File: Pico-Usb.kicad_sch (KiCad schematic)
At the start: 40 parts, among them J1 USB_A, J3 MEM2067-02-180-00-A_REVB, J4 10133475-10001LF, SW1 SW_Push, SW2 SW_Push, SW3 SW_Push, SW4 A6H-4101, U1 RP2040, U2 W25Q128JVS, U3 MAX40200AUK, U4 MAX40200AUK, U5 AP2112K-3.3, U6 TS3USB221ARSER, Y2 ABM3B-12.000MHZ-10-1-U-T

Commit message: Elimine todas las pistas y acomode los componetes
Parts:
- renumbered SW2 to BOOTSEL, SW3 to MODE, SW1 to RST
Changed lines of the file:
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@@
 		(dnp no)
 		(fields_autoplaced yes)
-		(property "Reference" "SW2"
+		(property "Reference" "BOOTSEL"
 			(at 182.88 69.85 0)
 			(show_name no)
@@
 			(project "Pico-Usb"
 				(path "/e96aad04-5f72-44f4-a95f-714a14090504"
-					(reference "SW2")
+					(reference "BOOTSEL")
 					(unit 1)
 				)
@@
 		(dnp no)
 		(fields_autoplaced yes)
-		(property "Reference" "SW1"
+		(property "Reference" "RST"
 			(at 39.37 132.08 0)
 			(show_name no)
@@
 			(project "Pico-Usb"
 				(path "/e96aad04-5f72-44f4-a95f-714a14090504"
-					(reference "SW1")
+					(reference "RST")
 					(unit 1)
 				)
@@
 		(dnp no)
 		(fields_autoplaced yes)
-		(property "Reference" "SW3"
-			(at 113.0299 123.19 90)
+		(property "Reference" "MODE"
+			(at 114.3 119.38 0)
 			(show_name no)
 			(do_not_autoplace no)
@@
 					(size 1.27 1.27)
 				)
-				(justify right)
 			)
 		)
 		(property "Value" "SW_Push"
-			(at 115.5699 123.19 90)
+			(at 114.3 121.92 0)
 			(show_name no)
 			(do_not_autoplace no)
@@
 					(size 1.27 1.27)
 				)
-				(justify right)
 			)
 		)
@@
 			(project "Pico-Usb"
 				(path "/e96aad04-5f72-44f4-a95f-714a14090504"
-					(reference "SW3")
+					(reference "MODE")
 					(unit 1)
 				)

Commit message: Termine el ruteo
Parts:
- renumbered SW4 to CFG
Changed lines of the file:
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@@
 		(dnp no)
 		(fields_autoplaced yes)
-		(property "Reference" "SW4"
+		(property "Reference" "CFG"
 			(at 205.7304 229.87 0)
 			(show_name no)
@@
 			(project "Pico-Usb"
 				(path "/e96aad04-5f72-44f4-a95f-714a14090504"
-					(reference "SW4")
+					(reference "CFG")
 					(unit 1)
 				)

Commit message: Corregi valores
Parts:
- C10, C11, C13: value 10μF -> 10uF
- C5, C7: value 1μF -> 1uF
- R2, R3: value 28 -> 28R
- R7, R8: value 5.1k -> 5k1
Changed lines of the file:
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@@
 			)
 		)
-		(property "Value" "28"
+		(property "Value" "28R"
 			(at 48.26 151.892 90)
 			(show_name no)
@@
 			)
 		)
-		(property "Value" "28"
+		(property "Value" "28R"
 			(at 48.26 145.288 90)
 			(show_name no)
@@
 			)
 		)
-		(property "Value" "5.1k"
+		(property "Value" "5k1"
 			(at 323.596 92.964 0)
 			(show_name no)
@@
 			)
 		)
-		(property "Value" "1μF"
+		(property "Value" "1uF"
 			(at 94.742 102.87 90)
 			(show_name no)
@@
 			)
 		)
-		(property "Value" "10μF"
+		(property "Value" "10uF"
 			(at 369.316 142.24 0)
 			(show_name no)
@@
 			)
 		)
-		(property "Value" "1μF"
+		(property "Value" "1uF"
 			(at 85.344 99.822 90)
 			(show_name no)
@@
 			)
 		)
-		(property "Value" "10μF"
+		(property "Value" "10uF"
 			(at 338.836 143.256 0)
 			(show_name no)
@@
 			)
 		)
-		(property "Value" "10μF"
+		(property "Value" "10uF"
 			(at 199.136 175.26 0)
 			(show_name no)
@@
 			)
 		)
-		(property "Value" "5.1k"
+		(property "Value" "5k1"
 			(at 377.444 108.966 0)
 			(show_name no)

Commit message: Corregi valores y pistas ground faltantes
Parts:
- renumbered BOOTSEL to BOOTSEL1, C6 to C1, C2 to C10, C12 to C11, C13 to C12, C1 to C13, C9 to C2, C8 to C3, C7 to C6, C3 to C7, C11 to C8, C10 to C9, CFG to CFG1, J4 to J2, MODE to MODE1, R6 to R1, R13 to R10, R1 to R11, R9 to R12, R10 to R13, R5 to R2, R7 to R3, R8 to R4, R4 to R5, R3 to R6, R2 to R7, R11 to R8, R12 to R9, RST to RST1, U3 to U1, U4 to U2, U2 to U3, U5 to U4, U1 to U5, Y2 to Y1

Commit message: Cambie el usb A
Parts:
- removed J1: USB_A, Connector_USB:USB_A_CNCTech_1001-011-01101_Horizontal, symbol Connector:USB_A
- added USB1: USB_AM_180-WT, Custom_Connectors:USB-AM-180-WT, symbol USB_AM_180-WT:USB_AM_180-WT
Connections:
- net GND: now also USB1.4 (GND), USB1.5 (SHELL), USB1.6 (SHELL)
- net USB_A_D+: now also USB1.3 (D+)
- net USB_A_D-: now also USB1.2 (D-)
- net at U1.1 (VDD), U1.3 (EN): now also USB1.1 (VBUS)
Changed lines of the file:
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@@
 	)
 	(junction
+		(at 316.23 34.29)
+		(diameter 0)
+		(color 0 0 0 0)
+	)
+	(junction
 		(at 367.03 39.37)
 		(diameter 0)
@@
 	)
 	(junction
+		(at 316.23 26.67)
+		(diameter 0)
+		(color 0 0 0 0)
+	)
+	(junction
 		(at 198.12 240.03)
 		(diameter 0)
@@
 	)
 	(junction
-		(at 331.47 39.37)
-		(diameter 0)
-		(color 0 0 0 0)
-	)
-	(junction
 		(at 25.4 170.18)
 		(diameter 0)
@@
 	(wire
 		(pts
-			(xy 339.09 24.13) (xy 364.49 24.13)
+			(xy 48.26 128.27) (xy 48.26 130.81)
 		)
 		(stroke
@@
 	(wire
 		(pts
-			(xy 48.26 128.27) (xy 48.26 130.81)
+			(xy 340.36 16.51) (xy 316.23 16.51)
 		)
 		(stroke
@@
 	(wire
 		(pts
+			(xy 339.09 34.29) (xy 364.49 34.29)
+		)
+		(stroke
+			(width 0)
+			(type default)
+		)
+	)
+	(wire
+		(pts
 			(xy 224.79 163.83) (xy 224.79 168.91)
 		)
@@
 	(wire
 		(pts
+			(xy 339.09 26.67) (xy 340.36 26.67)
+		)
+		(stroke
+			(width 0)
+			(type default)
+		)
+	)
+	(wire
+		(pts
 			(xy 364.49 24.13) (xy 370.84 24.13)
 		)
@@
 	(wire
 		(pts
+			(xy 364.49 34.29) (xy 364.49 24.13)
+		)
+		(stroke
+			(width 0)
+			(type default)
+		)
+	)
+	(wire
+		(pts
 			(xy 43.18 187.96) (xy 43.18 193.04)
 		)
@@
 	(wire
 		(pts
+			(xy 340.36 26.67) (xy 340.36 16.51)
+		)
+		(stroke
+			(width 0)
+			(type default)
+		)
+	)
+	(wire
+		(pts
 			(xy 336.55 149.86) (xy 344.17 149.86)
 		)
@@
 	(wire
 		(pts
+			(xy 316.23 34.29) (xy 316.23 39.37)
+		)
+		(stroke
+			(width 0)
+			(type default)
+		)
+	)
+	(wire
+		(pts
 			(xy 78.74 111.76) (xy 78.74 106.68)
 		)
@@
 	(wire
 		(pts
-			(xy 331.47 39.37) (xy 367.03 39.37)
-		)
-		(stroke
-			(width 0)
-			(type default)
-		)
-	)
-	(wire
-		(pts
 			(xy 83.82 114.3) (xy 83.82 111.76)
 		)
@@
 	(wire
 		(pts
+			(xy 316.23 16.51) (xy 316.23 26.67)
+		)
+		(stroke
+			(width 0)
+			(type default)
+		)
+	)
+	(wire
+		(pts
 			(xy 83.82 111.76) (xy 83.82 106.68)
 		)
@@
 	(wire
 		(pts
-			(xy 88.9 115.57) (xy 86.36 115.57)
+			(xy 316.23 39.37) (xy 367.03 39.37)
 		)
 		(stroke
@@
 	(wire
 		(pts
-			(xy 372.11 27.94) (xy 372.11 30.48)
+			(xy 88.9 115.57) (xy 86.36 115.57)
 		)
 		(stroke
@@
 		)
 	)
-	(polyline
+	(wire
 		(pts
-			(xy 300.99 125.73) (xy 408.94 125.73)
+			(xy 372.11 27.94) (xy 372.11 30.48)
 		)
 		(stroke
@@
 		)
 	)
-	(wire
+	(polyline
 		(pts
-			(xy 212.09 181.61) (xy 209.55 181.61)
+			(xy 300.99 125.73) (xy 408.94 125.73)
 		)
 		(stroke
@@
 	(wire
 		(pts
-			(xy 328.93 97.79) (xy 332.74 97.79)
+			(xy 212.09 181.61) (xy 209.55 181.61)
 		)
 		(stroke
@@
 	(wire
 		(pts
-			(xy 328.93 39.37) (xy 331.47 39.37)
+			(xy 328.93 97.79) (xy 332.74 97.79)
 		)
 		(stroke
@@
 	(wire
 		(pts
+			(xy 316.23 26.67) (xy 316.23 34.29)
+		)
+		(stroke
+			(width 0)
+			(type default)
+		)
+	)
+	(wire
+		(pts
 			(xy 88.9 105.41) (xy 88.9 83.82)
 		)
@@
 	)
 	(symbol
-		(lib_id "Connector:USB_A")
-		(at 331.47 29.21 0)
-		(unit 1)
-		(body_style 1)
-		(exclude_from_sim no)
-		(in_bom yes)
-		(on_board yes)
-		(in_pos_files yes)
-		(dnp no)
-		(fields_autoplaced yes)
-		(property "Reference" "J1"
-			(at 331.47 16.51 0)
-			(show_name no)
-			(do_not_autoplace no)
-			(effects
-				(font
-					(size 1.27 1.27)
-				)
-			)
-		)
-		(property "Value" "USB_A"
-			(at 331.47 19.05 0)
-			(show_name no)
-			(do_not_autoplace no)
-			(effects
-				(font
-					(size 1.27 1.27)
-				)
-			)
-		)
-		(property "Footprint" "Connector_USB:USB_A_CNCTech_1001-011-01101_Horizontal"
-			(at 335.28 30.48 0)
-			(hide yes)
-			(show_name no)
-			(do_not_autoplace no)
-			(effects
-				(font
-					(size 1.27 1.27)
-				)
-			)
-		)
-		(property "Datasheet" ""
-			(at 335.28 30.48 0)
-			(hide yes)
-			(show_name no)
-			(do_not_autoplace no)
-			(effects
-				(font
-					(size 1.27 1.27)
-				)
-			)
-		)
-		(property "Description" "USB Type A connector"
-			(at 331.47 29.21 0)
-			(hide yes)
-			(show_name no)
-			(do_not_autoplace no)
-			(effects
-				(font
-					(size 1.27 1.27)
-				)
-			)
-		)
-		(pin "4"
-		)
-		(pin "3"
-		)
-		(pin "1"
-		)
-		(pin "2"
-		)
-		(pin "SH"
-		)
-		(instances
-			(project "Pico-Usb"
-				(path "/e96aad04-5f72-44f4-a95f-714a14090504"
-					(reference "J1")
-					(unit 1)
-				)
-			)
-		)
-	)
-	(symbol
 		(lib_id "Device:R")
 		(at 48.26 149.86 270)
@@
 					(unit 1)
 				)
+			)
+		)
+	)
+	(symbol
+		(lib_id "USB_AM_180-WT:USB_AM_180-WT")
+		(at 327.66 30.48 180)
+		(unit 1)
+		(body_style 1)
+		(exclude_from_sim no)
+		(in_bom yes)
+		(on_board yes)
+		(in_pos_files yes)
+		(dnp no)
+		(fields_autoplaced yes)
+		(property "Reference" "USB1"
+			(at 327.66 19.05 0)
+			(show_name no)
+			(do_not_autoplace no)
+			(effects
+				(font
+					(size 1.27 1.27)
+				)
+			)
+		)
+		(property "Value" "USB_AM_180-WT"
+			(at 327.66 21.59 0)
+			(show_name no)
+			(do_not_autoplace no)
+			(effects
+				(font
+					(size 1.27 1.27)
+				)
+			)
+		)
+		(property "Footprint" "Custom_Connectors:USB-AM-180-WT"
+			(at 327.152 37.846 0)
+			(hide yes)
+			(show_name no)
+			(do_not_autoplace no)
+			(effects
+				(font
+					(size 1.27 1.27)
+				)
+			)
+		)
+		(property "Datasheet" ""
+			(at 327.66 30.48 0)
+			(hide yes)
+			(show_name no)
+			(do_not_autoplace no)
+			(effects
+				(font
+					(size 1.27 1.27)
+				)
+			)
+		)
+		(property "Description" ""
+			(at 327.66 30.48 0)
+			(hide yes)
+			(show_name no)
+			(do_not_autoplace no)
+			(effects
+				(font
+					(size 1.27 1.27)
+				)
+			)
+		)
+		(property "Manufacturer Part" ""
+			(at 327.152 39.878 0)
+			(hide yes)
+			(show_name no)
+			(do_not_autoplace no)
+			(effects
+				(font
+					(size 1.27 1.27)
+				)
+			)
+		)
+		(property "Manufacturer" ""
+			(at 311.658 41.148 0)
+			(hide yes)
+			(show_name no)
+			(do_not_autoplace no)
+			(effects
+				(font
+					(size 1.27 1.27)
+				)
+			)
+		)
+		(property "Supplier Part" "C54110164"
+			(at 327.406 22.86 0)
+			(hide yes)
+			(show_name no)
+			(do_not_autoplace no)
+			(effects
+				(font
+					(size 1.27 1.27)
+				)
+			)
+		)
+		(property "Supplier" "LCSC"
+			(at 327.66 20.828 0)
+			(hide yes)
+			(show_name no)
+			(do_not_autoplace no)
+			(effects
+				(font
+					(size 1.27 1.27)
+				)
+			)
+		)
+		(pin "2"
+		)
+		(pin "5"
+		)
+		(pin "6"
+		)
+		(pin "1"
+		)
+		(pin "4"
+		)
+		(pin "3"
+		)
+		(instances
+			(project "Pico-Usb"
+				(path "/e96aad04-5f72-44f4-a95f-714a14090504"
+					(reference "USB1")
+					(unit 1)
+				)

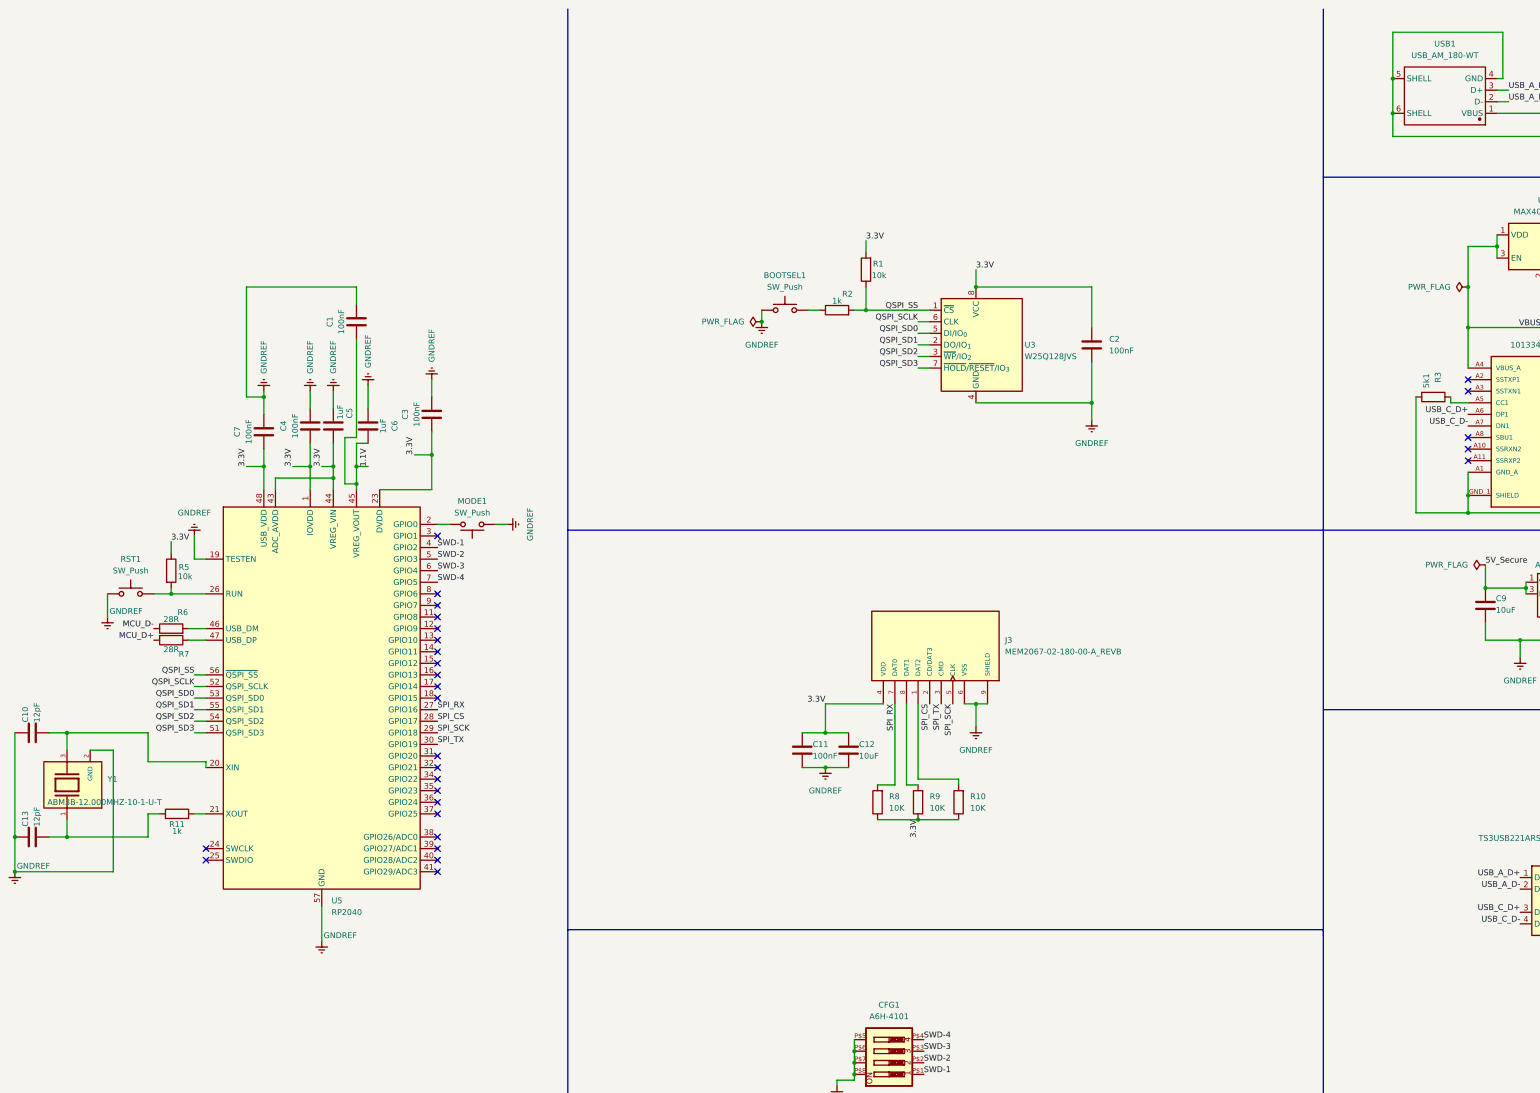
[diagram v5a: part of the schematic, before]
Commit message: Modifique los componentes originales por unos que si se encuentran
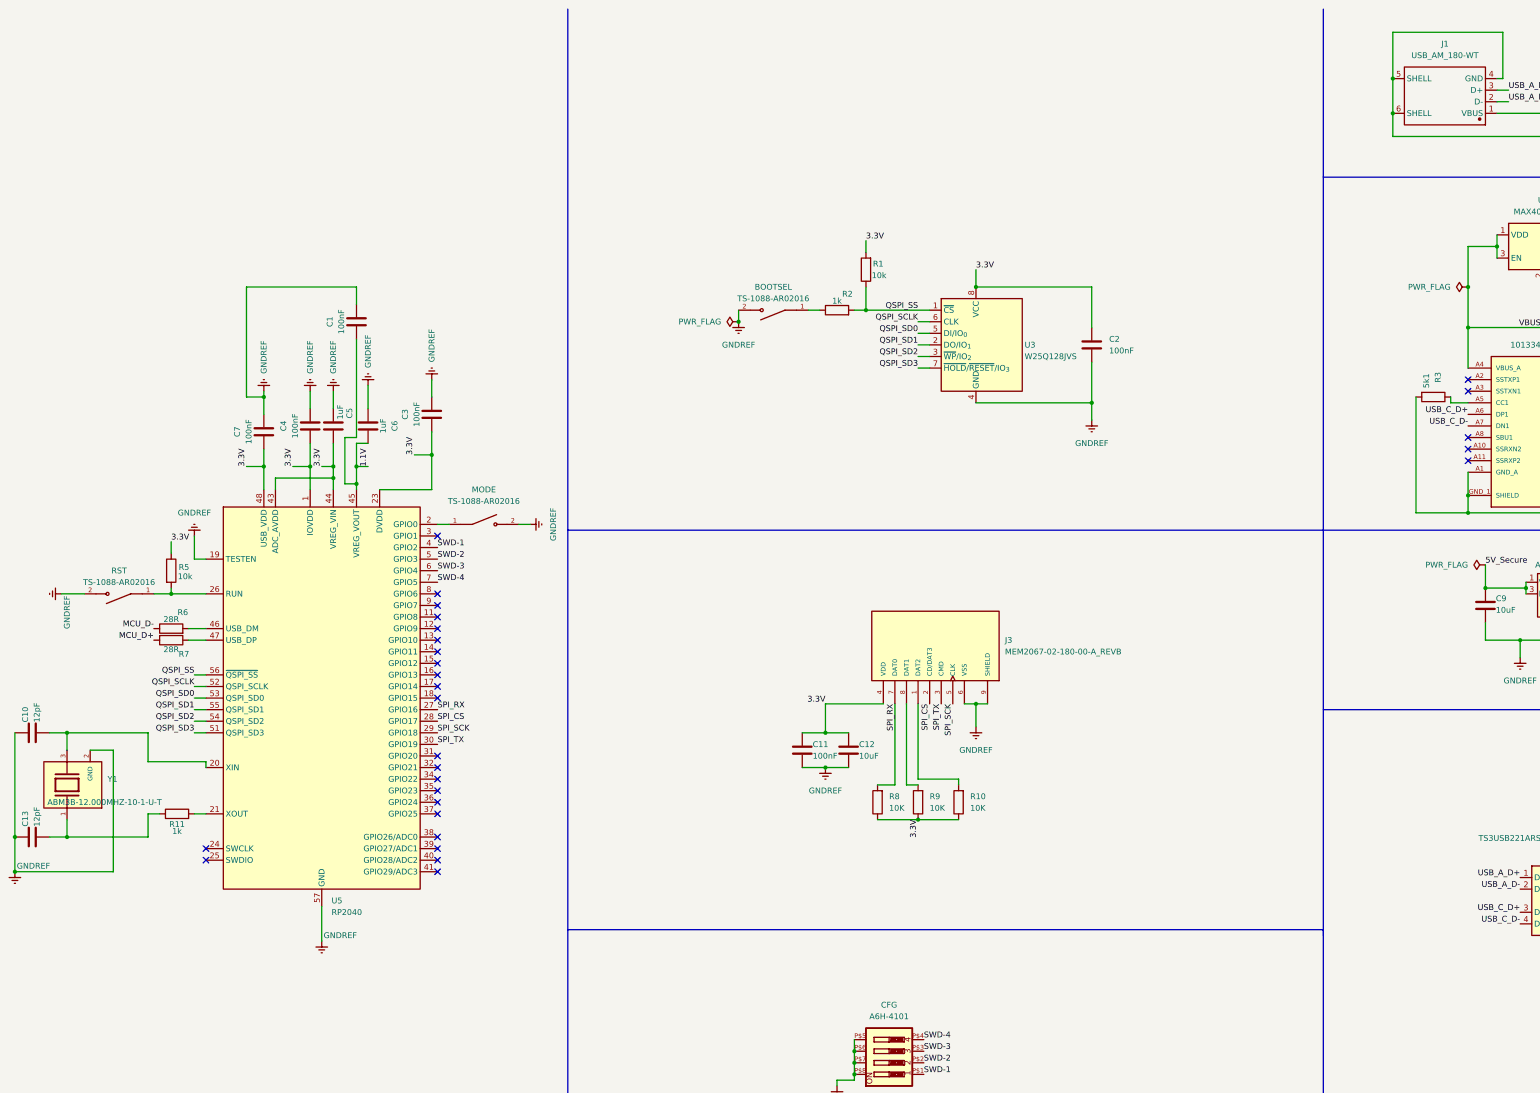
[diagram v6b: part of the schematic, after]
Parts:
- removed BOOTSEL1, MODE1, RST1: SW_Push, Button_Switch_SMD:SW_Push_SPST_NO_Alps_SKRK, symbol Switch:SW_Push
- added BOOTSEL, MODE, RST: TS-1088-AR02016, Custom_Switchs:SW_TS-1088-AR02016, symbol TS-1088-AR02016:TS-1088-AR02016
- renumbered CFG1 to CFG, USB1 to J1
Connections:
- net GND: now also BOOTSEL.2, MODE.2, RST.2
- net at R5.2, U5.26 (RUN): now also RST.1
- net at R2.1: now also BOOTSEL.1
- net at U5.2 (GPIO0): now also MODE.1
